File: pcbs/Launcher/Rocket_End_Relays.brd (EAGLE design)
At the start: 41 parts, among them IC2 LM2576T-ADJ, J1 22-27-2021-02, K4 LD105, K5 LD105, K6 LD105, K7 LD105, T1 BC547, T2 BC547, T3 BC547, T4 BC547, T5 BC547, U1 ARDUINO-MEGAPRO-5V, X1 1751248, X2 22-23-2041, X3 22-23-2021, X4 1751248, X5 22-23-2021

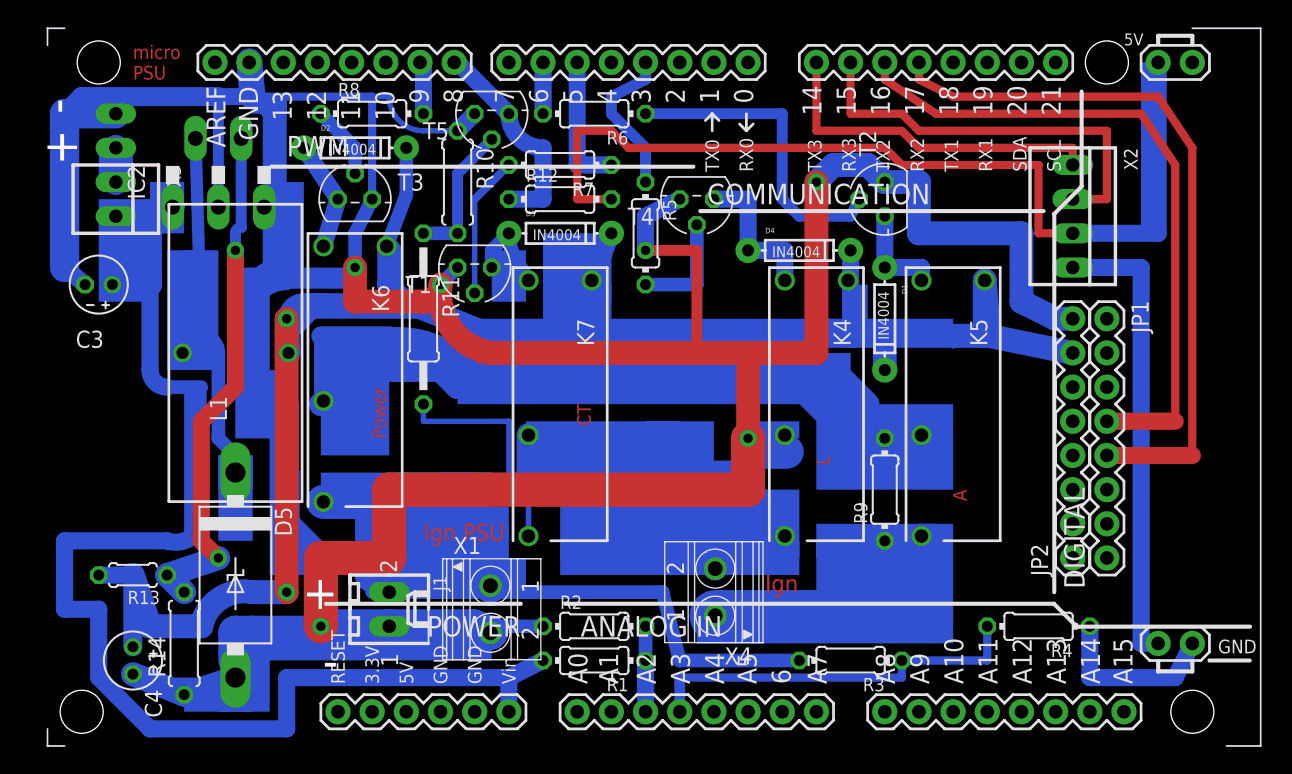
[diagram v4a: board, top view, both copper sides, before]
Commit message: * Adding my own updated library of sparkfun stuff.
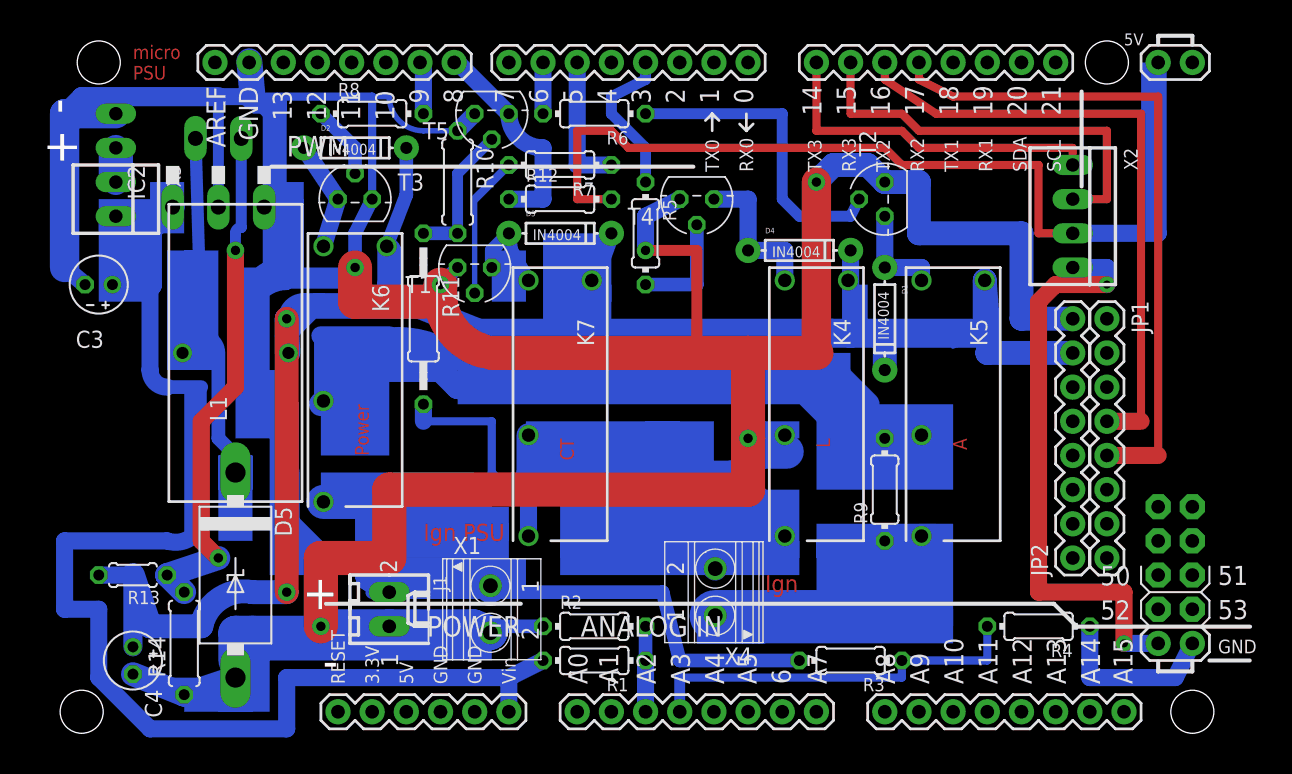
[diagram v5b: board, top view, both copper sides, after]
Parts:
- U1: device JoeMega_Ether_Edited:ARDUINO_MEGA-PRO-5V -> Joe_SparkFun-Boards:ARDUINO_MEGA-PRO-5V
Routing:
- net N$16: track 34.3 -> 43.7 mm, vias 0 -> 2
- net N$2: track 53.1 -> 49.8 mm
- net N$1: track 49.8 -> 46.5 mm
- net N$30: track 17.6 -> 16.1 mm
- net N$5: track 167.8 -> 169.1 mm
- net N$33: track 346.0 -> 347.0 mm

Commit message: * making more space at PSU side of board for cut.
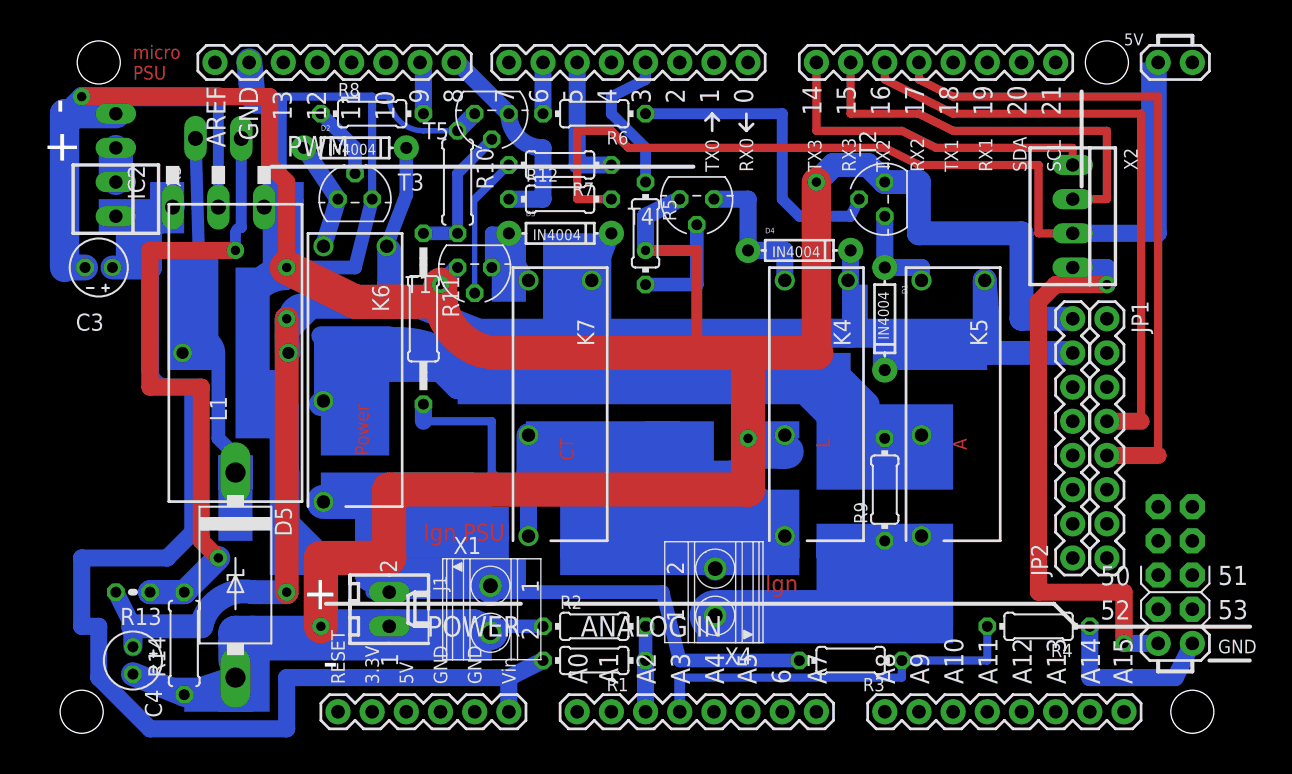
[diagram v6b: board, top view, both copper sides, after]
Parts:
- R13: device rcl:0204/5 -> resistor:0204V
- moved C3 1.27 mm to (7.62, 43.2)
- moved R13 1.27 mm to (10.2, 19.1)
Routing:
- net N$33: track 347.0 -> 380.7 mm, vias 6 -> 7
- net N$37: track 38.8 -> 50.7 mm
- net N$5: track 169.1 -> 162.8 mm
- net VCC: track 98.8 -> 95.7 mm
- net N$29: track 45.7 -> 47.0 mm
- net N$20: track 6.92 -> 7.66 mm

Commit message: * Removed some parts from Joe_Sparkfun-boards.lbf * A bit of a small tidy up on board relays
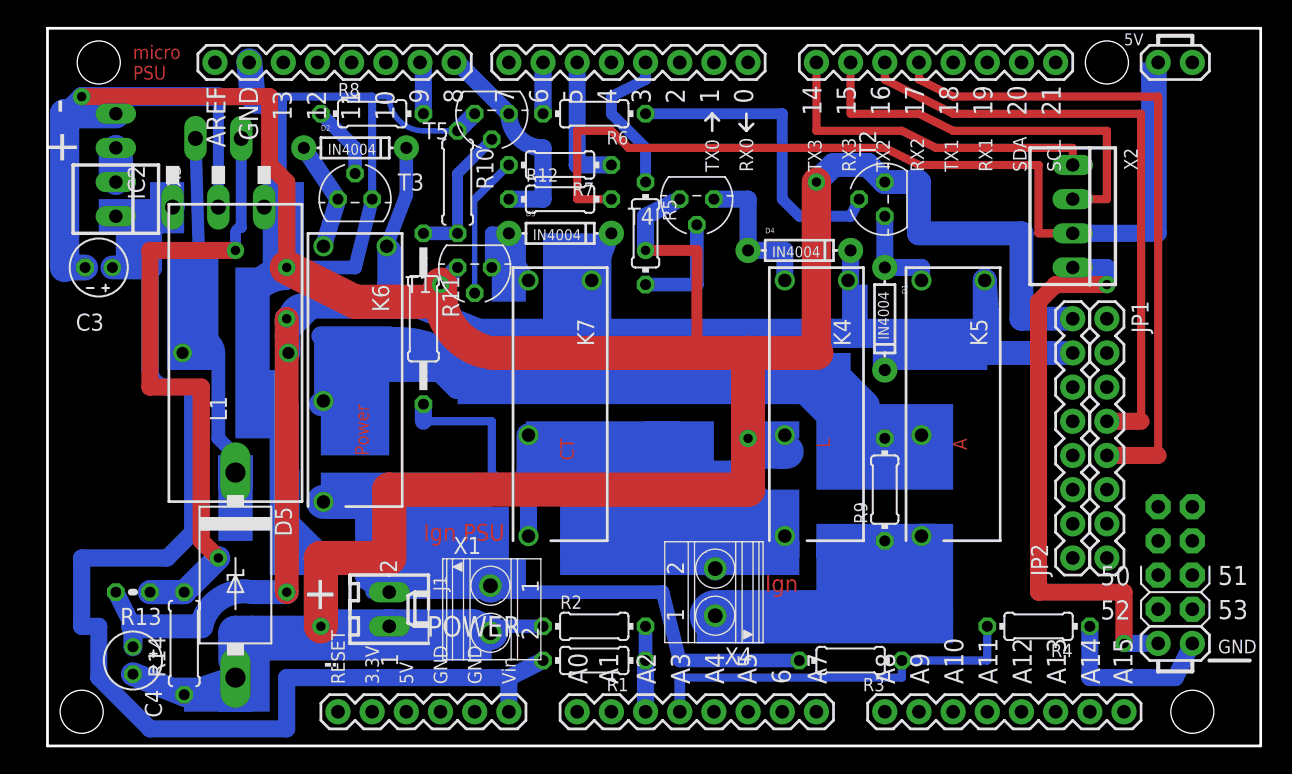
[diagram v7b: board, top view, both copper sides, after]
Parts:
- X3: value 22-23-2021 -> (none)
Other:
- board outline added: 90.2 x 53.3 mm
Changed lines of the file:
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@@
 <rectangle x1="41.91" y1="21.59" x2="49.53" y2="27.94" layer="16"/>
 <rectangle x1="16.51" y1="10.16" x2="19.05" y2="12.7" layer="16"/>
-<text x="25.4" y="12.7" size="2.54" layer="20" rot="MR0">-</text>
-<text x="25.4" y="17.78" size="2.54" layer="20" rot="MR0">+</text>
-<text x="3.81" y="54.61" size="2.54" layer="20" rot="MR90">-</text>
-<text x="3.81" y="50.8" size="2.54" layer="20" rot="MR90">+</text>
+<text x="25.4" y="12.7" size="2.54" layer="21" rot="MR0">-</text>
+<text x="25.4" y="17.78" size="2.54" layer="21" rot="MR0">+</text>
+<text x="3.81" y="54.61" size="2.54" layer="21" rot="MR90">-</text>
+<text x="3.81" y="50.8" size="2.54" layer="21" rot="MR90">+</text>
 <text x="57.15" y="19.05" size="1.27" layer="1">Ign</text>
 <rectangle x1="24.13" y1="25.4" x2="35.56" y2="27.94" layer="16"/>
@@
 <element name="D4" library="SparkFun-DiscreteSemi" package="DIODE-1N4148" value="IN4004" x="59.69" y="44.45"/>
 <element name="IC2" library="LM2576" package="TO220-5" value="LM2576T-ADJ" x="16.51" y="55.88"/>
-<element name="X3" library="con-molex" package="22-23-2021" value="22-23-2021" x="8.89" y="53.34" smashed="yes" rot="MR90">
+<element name="X3" library="con-molex" package="22-23-2021" value="" x="8.89" y="53.34" rot="MR90">
 <attribute name="OC_NEWARK" value="25C3832" x="8.89" y="53.34" size="1.778" layer="28" rot="MR90" display="off"/>
 <attribute name="MPN" value="22-23-2021" x="8.89" y="53.34" size="1.778" layer="28" rot="MR90" display="off"/>
 <attribute name="MF" value="MOLEX" x="8.89" y="53.34" size="1.778" layer="28" rot="MR90" display="off"/>
 <attribute name="OC_FARNELL" value="1462926" x="8.89" y="53.34" size="1.778" layer="28" rot="MR90" display="off"/>
-<attribute name="NAME" x="12.7" y="50.8" size="1.016" layer="26" ratio="10" rot="MR90"/>
 </element>
 <element name="C3" library="rcl" package="E2-4" value="100uF 16V" x="7.62" y="43.18" smashed="yes" rot="R180">
